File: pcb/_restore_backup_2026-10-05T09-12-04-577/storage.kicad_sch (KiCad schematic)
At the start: 5 parts, among them Y1 Crystal_GND24

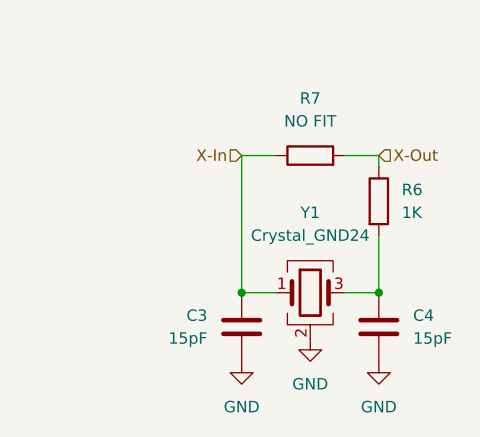
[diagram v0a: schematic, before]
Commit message: making the power delivery
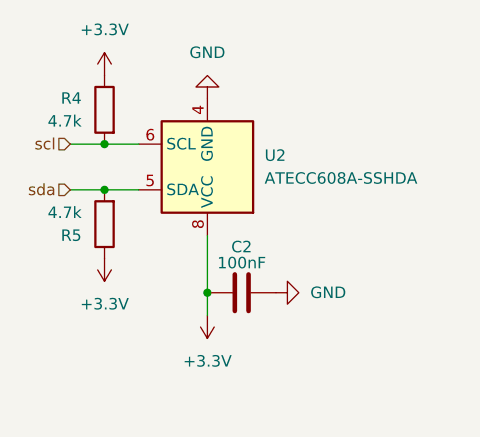
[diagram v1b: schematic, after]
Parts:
- removed C3, C4: 15pF, Package_SON:Winbond_USON-8-1EP_3x2mm_P0.5mm_EP0.2x1.6mm, symbol Device:C
- removed R6: 1K, Package_DIP:DIP-8_W7.62mm, symbol Device:R
- removed R7: NO FIT, symbol Device:R
- removed Y1: Crystal_GND24, symbol Device:Crystal_GND24
- added C2: 100nF, Package_SON:Winbond_USON-8-1EP_3x2mm_P0.5mm_EP0.2x1.6mm, symbol Device:C
- added R4, R5: 4.7k, Package_DIP:DIP-8_W7.62mm, symbol Device:R
- added U2: ATECC608A-SSHDA, Package_SO:SOIC-8_3.9x4.9mm_P1.27mm, symbol Security:ATECC608A-SSHDA
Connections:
- net GND: now also C2.2, U2.4 (GND)
- new net +3.3V: C2.1, R4.1, R5.1, U2.8 (VCC)
- new net scl: R4.2, U2.6 (SCL)
- new net sda: R5.2, U2.5 (SDA)
